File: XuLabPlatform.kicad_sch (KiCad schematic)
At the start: 9 parts, among them J10 Servo7, J11 Servo8, J12 Thruster SGN, J4 Servo1, J5 Servo2, J6 Servo3, J7 Servo4, J8 Servo5, J9 Servo6

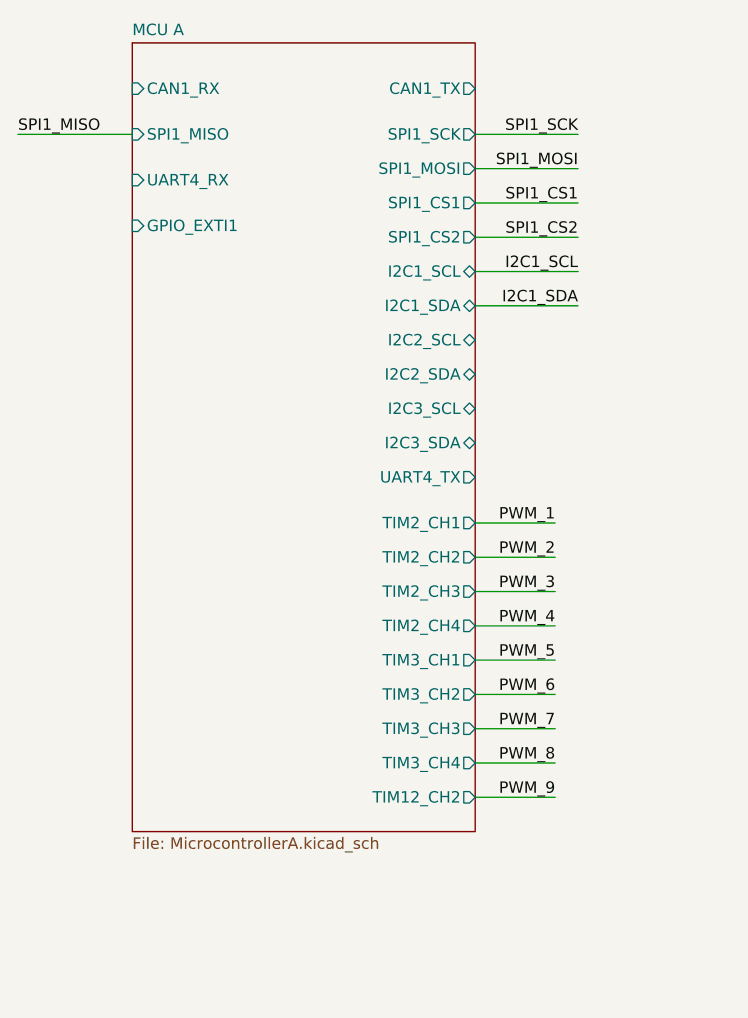
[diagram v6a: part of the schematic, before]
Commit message: Remove unused I2C pins and add USB
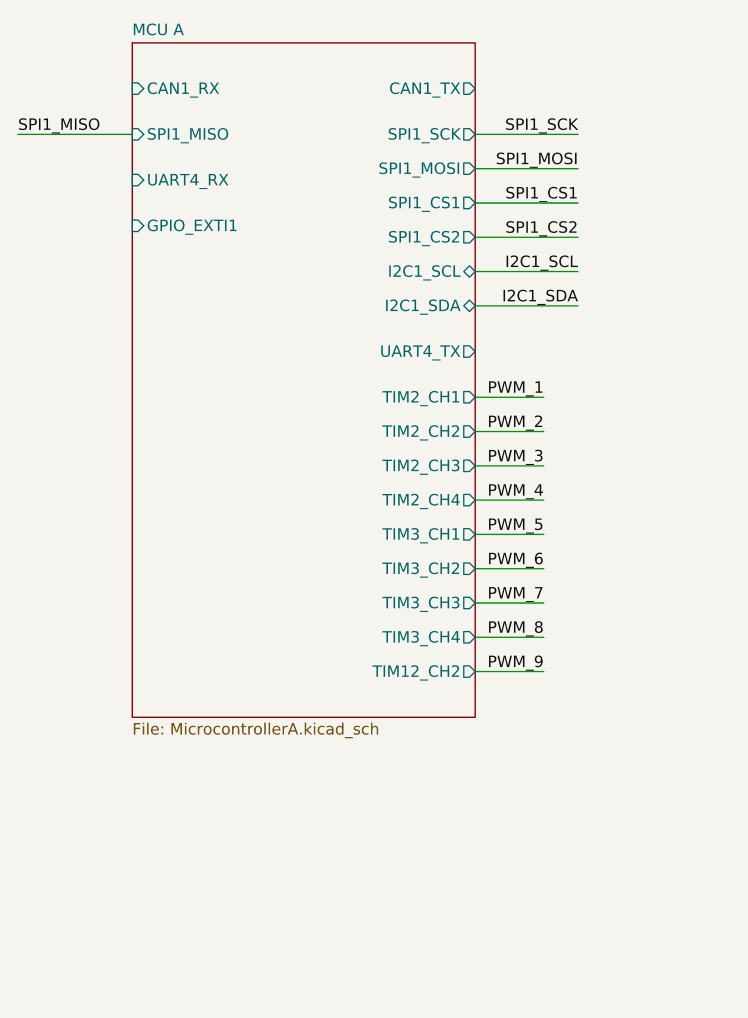
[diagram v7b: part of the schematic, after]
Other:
- sheet MCU A ports: added none; removed I2C2_SCL, I2C2_SDA, I2C3_SCL, I2C3_SDA
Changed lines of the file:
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@@
 	(wire
 		(pts
-			(xy 88.9 99.06) (xy 97.79 99.06)
+			(xy 88.9 85.09) (xy 96.52 85.09)
 		)
 		(stroke
@@
 	(wire
 		(pts
-			(xy 88.9 91.44) (xy 97.79 91.44)
+			(xy 88.9 77.47) (xy 96.52 77.47)
 		)
 		(stroke
@@
 	(wire
 		(pts
-			(xy 88.9 102.87) (xy 97.79 102.87)
+			(xy 88.9 88.9) (xy 96.52 88.9)
 		)
 		(stroke
@@
 	(wire
 		(pts
-			(xy 88.9 118.11) (xy 97.79 118.11)
+			(xy 88.9 104.14) (xy 96.52 104.14)
 		)
 		(stroke
@@
 	(wire
 		(pts
-			(xy 88.9 121.92) (xy 97.79 121.92)
+			(xy 88.9 107.95) (xy 96.52 107.95)
 		)
 		(stroke
@@
 	(wire
 		(pts
-			(xy 88.9 106.68) (xy 97.79 106.68)
-		)
-		(stroke
-			(width 0)
-			(type default)
-		)
-	)
-	(wire
-		(pts
-			(xy 88.9 110.49) (xy 97.79 110.49)
+			(xy 88.9 92.71) (xy 96.52 92.71)
+		)
+		(stroke
+			(width 0)
+			(type default)
+		)
+	)
+	(wire
+		(pts
+			(xy 88.9 96.52) (xy 96.52 96.52)
 		)
 		(stroke
@@
 	(wire
 		(pts
-			(xy 88.9 95.25) (xy 97.79 95.25)
+			(xy 88.9 81.28) (xy 96.52 81.28)
 		)
 		(stroke
@@
 	(wire
 		(pts
-			(xy 88.9 114.3) (xy 97.79 114.3)
+			(xy 88.9 100.33) (xy 96.52 100.33)
 		)
 		(stroke
@@
 	)
 	(label "PWM_8"
-		(at 97.79 118.11 180)
+		(at 96.52 104.14 180)
 		(effects
 			(font
@@
 	)
 	(label "PWM_5"
-		(at 97.79 106.68 180)
+		(at 96.52 92.71 180)
 		(effects
 			(font
@@
 	)
 	(label "PWM_9"
-		(at 97.79 121.92 180)
+		(at 96.52 107.95 180)
 		(effects
 			(font
@@
 	)
 	(label "PWM_4"
-		(at 97.79 102.87 180)
+		(at 96.52 88.9 180)
 		(effects
 			(font
@@
 	)
 	(label "PWM_7"
-		(at 97.79 114.3 180)
+		(at 96.52 100.33 180)
 		(effects
 			(font
@@
 	)
 	(label "PWM_2"
-		(at 97.79 95.25 180)
+		(at 96.52 81.28 180)
 		(effects
 			(font
@@
 	)
 	(label "PWM_1"
-		(at 97.79 91.44 180)
+		(at 96.52 77.47 180)
 		(effects
 			(font
@@
 	)
 	(label "PWM_6"
-		(at 97.79 110.49 180)
+		(at 96.52 96.52 180)
 		(effects
 			(font
@@
 	)
 	(label "PWM_3"
-		(at 97.79 99.06 180)
+		(at 96.52 85.09 180)
 		(effects
 			(font
@@
 	(sheet
 		(at 50.8 38.1)
-		(size 38.1 87.63)
+		(size 38.1 74.93)
 		(exclude_from_sim no)
 		(in_bom yes)
@@
 		)
 		(property "Sheetfile" "MicrocontrollerA.kicad_sch"
-			(at 50.8 126.3146 0)
+			(at 50.8 113.6146 0)
 			(effects
 				(font
@@
 			)
 		)
-		(pin "I2C2_SCL" bidirectional
-			(at 88.9 71.12 0)
-			(effects
-				(font
-					(size 1.27 1.27)
-				)
-				(justify right)
-			)
-		)
-		(pin "I2C2_SDA" bidirectional
-			(at 88.9 74.93 0)
-			(effects
-				(font
-					(size 1.27 1.27)
-				)
-				(justify right)
-			)
-		)
-		(pin "I2C3_SCL" bidirectional
-			(at 88.9 78.74 0)
-			(effects
-				(font
-					(size 1.27 1.27)
-				)
-				(justify right)
-			)
-		)
-		(pin "I2C3_SDA" bidirectional
-			(at 88.9 82.55 0)
-			(effects
-				(font
-					(size 1.27 1.27)
-				)
-				(justify right)
-			)
-		)
 		(pin "SPI1_MISO" input
 			(at 50.8 48.26 180)
@@
 		)
 		(pin "TIM2_CH1" output
-			(at 88.9 91.44 0)
+			(at 88.9 77.47 0)
 			(effects
 				(font
@@
 		)
 		(pin "TIM2_CH2" output
-			(at 88.9 95.25 0)
+			(at 88.9 81.28 0)
 			(effects
 				(font
@@
 		)
 		(pin "TIM2_CH3" output
-			(at 88.9 99.06 0)
+			(at 88.9 85.09 0)
 			(effects
 				(font
@@
 		)
 		(pin "TIM2_CH4" output
-			(at 88.9 102.87 0)
+			(at 88.9 88.9 0)
 			(effects
 				(font
@@
 		)
 		(pin "TIM3_CH1" output
-			(at 88.9 106.68 0)
+			(at 88.9 92.71 0)
 			(effects
 				(font
@@
 		)
 		(pin "TIM3_CH2" output
-			(at 88.9 110.49 0)
+			(at 88.9 96.52 0)
 			(effects
 				(font
@@
 		)
 		(pin "TIM3_CH3" output
-			(at 88.9 114.3 0)
+			(at 88.9 100.33 0)
 			(effects
 				(font
@@
 		)
 		(pin "TIM3_CH4" output
-			(at 88.9 118.11 0)
+			(at 88.9 104.14 0)
 			(effects
 				(font
@@
 		)
 		(pin "UART4_TX" output
-			(at 88.9 86.36 0)
+			(at 88.9 72.39 0)
 			(effects
 				(font
@@
 		)
 		(pin "TIM12_CH2" output
-			(at 88.9 121.92 0)
-			(effects
-				(font
+			(at 88.9 107.95 0)
+			(effects
+				(font

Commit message: Add footprints to symbols
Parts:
- J10, J11, J4, J5, J6, J7, J8, J9: Listing (none) -> https://www.digikey.com/en/products/detail/phoenix-contact/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
- J12: footprint Connector_PinHeader_2.54mm:PinHeader_1x03_P2.54mm_Vertical -> Connector_JST:JST_VH_B3P-VH_1x03_P3.96mm_Vertical; Listing (none) -> https://www.digikey.com/en/products/detail/jst-sales-americ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
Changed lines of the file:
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@@
+			)
+		)
+		(property "Listing" "https://www.digikey.com/en/products/detail/phoenix-contact/1715734/260632"
+			(at 214.63 146.05 0)
+			(effects
+				(font
+					(size 1.27 1.27)
+				)
+				(hide yes)
 			)
 		)
@@
 			)
 		)
+		(property "Listing" "https://www.digikey.com/en/products/detail/phoenix-contact/1715734/260632"
+			(at 189.23 129.54 0)
+			(effects
+				(font
+					(size 1.27 1.27)
+				)
+				(hide yes)
+			)
+		)
 		(pin "1"
 		)
@@
 			)
 		)
+		(property "Listing" "https://www.digikey.com/en/products/detail/phoenix-contact/1715734/260632"
+			(at 189.23 146.05 0)
+			(effects
+				(font
+					(size 1.27 1.27)
+				)
+				(hide yes)
+			)
+		)
 		(pin "1"
 		)
@@
 			)
 		)
+		(property "Listing" "https://www.digikey.com/en/products/detail/phoenix-contact/1715734/260632"
+			(at 240.03 146.05 0)
+			(effects
+				(font
+					(size 1.27 1.27)
+				)
+				(hide yes)
+			)
+		)
 		(pin "1"
 		)
@@
 			)
 		)
+		(property "Listing" "https://www.digikey.com/en/products/detail/phoenix-contact/1715734/260632"
+			(at 214.63 129.54 0)
+			(effects
+				(font
+					(size 1.27 1.27)
+				)
+				(hide yes)
+			)
+		)
 		(pin "1"
 		)
@@
 			)
 		)
+		(property "Listing" "https://www.digikey.com/en/products/detail/phoenix-contact/1715734/260632"
+			(at 265.43 129.54 0)
+			(effects
+				(font
+					(size 1.27 1.27)
+				)
+				(hide yes)
+			)
+		)
 		(pin "1"
 		)
@@
 			)
 		)
+		(property "Listing" "https://www.digikey.com/en/products/detail/phoenix-contact/1715734/260632"
+			(at 238.76 129.54 0)
+			(effects
+				(font
+					(size 1.27 1.27)
+				)
+				(hide yes)
+			)
+		)
 		(pin "1"
 		)
@@
 			)
 		)
-		(property "Footprint" "Connector_PinHeader_2.54mm:PinHeader_1x03_P2.54mm_Vertical"
+		(property "Footprint" "Connector_JST:JST_VH_B3P-VH_1x03_P3.96mm_Vertical"
 			(at 265.43 111.76 0)
 			(effects
@@
 			)
 		)
-		(property "Datasheet" "~"
+		(property "Datasheet" "https://www.jst-mfg.com/product/pdf/eng/eVH.pdf"
 			(at 265.43 111.76 0)
 			(effects
@@
 			)
 		)
+		(property "Listing" "https://www.digikey.com/en/products/detail/jst-sales-america-inc/B3P-VH/926548"
+			(at 265.43 111.76 0)
+			(effects
+				(font
+					(size 1.27 1.27)
+				)
+				(hide yes)
+			)
+		)
 		(pin "2"
 		)
@@
 			(at 265.43 146.05 0)
 			(effects
+				(font
+					(size 1.27 1.27)
+				)
+				(hide yes)
+			)
+		)
+		(property "Listing" "https://www.digikey.com/en/products/detail/phoenix-contact/1715734/260632"
+			(at 265.43 146.05 0)
+			(effects
